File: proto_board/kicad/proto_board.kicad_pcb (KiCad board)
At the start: 2 copper layers, 66 x 100 mm, 3 parts, among them J1 pcie_98, J2 Conn_02x25_Odd_Even, J3 Conn_02x25_Odd_Even

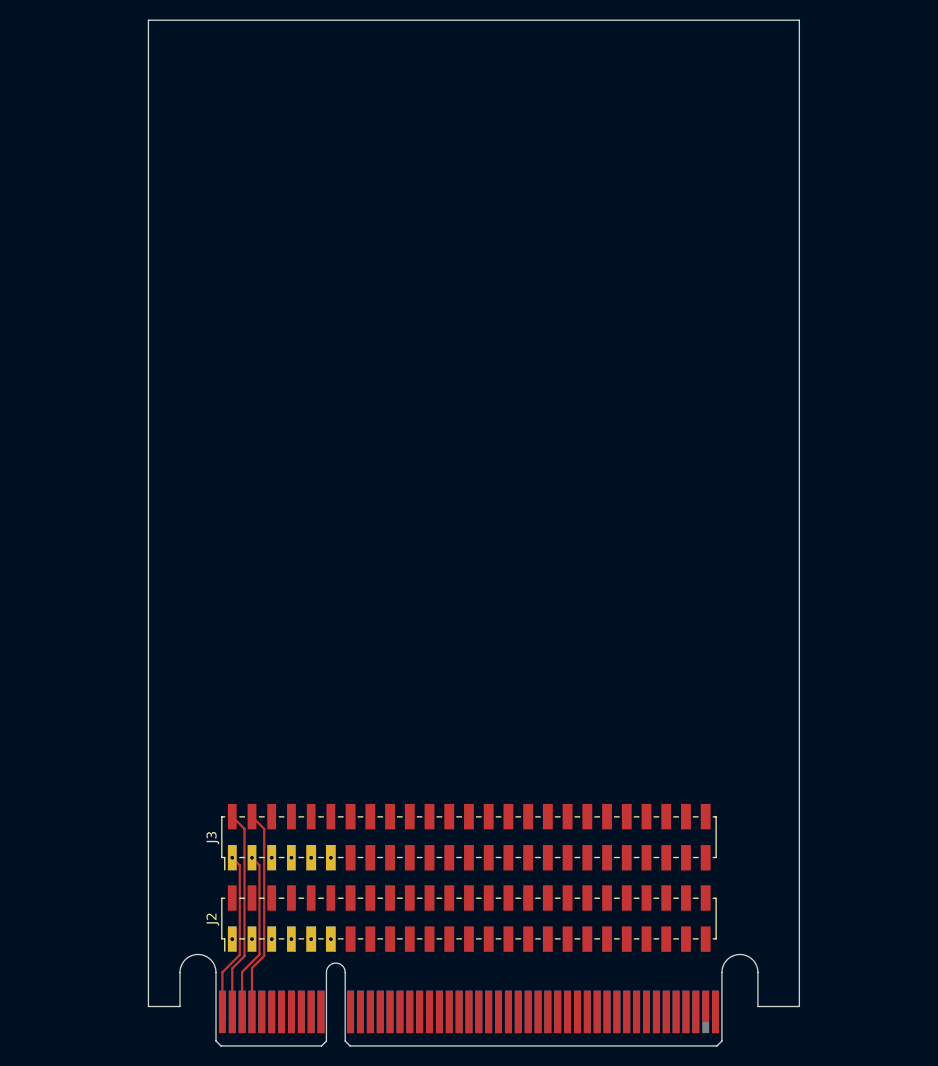
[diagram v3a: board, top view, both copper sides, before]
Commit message: Resized the proto board and added pads grid.
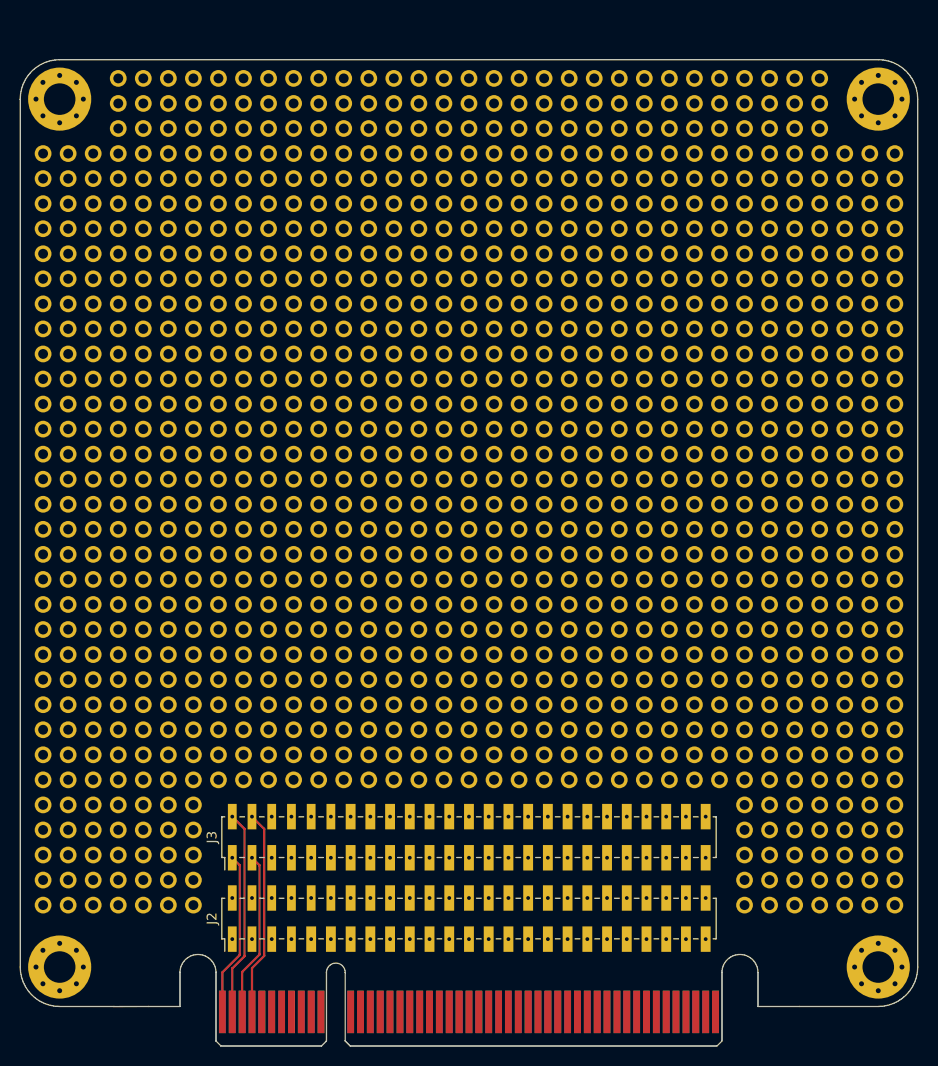
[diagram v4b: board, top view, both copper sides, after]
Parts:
- added H1: MountingHole, MountingHole:MountingHole_3.2mm_M3_Pad_Via, F.Cu at (-28.0, -96.0)
- added H2: MountingHole, MountingHole:MountingHole_3.2mm_M3_Pad_Via, F.Cu at (55.0, -96.0)
- added H3: MountingHole, MountingHole:MountingHole_3.2mm_M3_Pad_Via, F.Cu at (-28.0, -8.00)
- added H4: MountingHole, MountingHole:MountingHole_3.2mm_M3_Pad_Via, F.Cu at (55.0, -8.00)
- added REF**: pad, proto_board:pad, F.Cu at (26.2, -70.2)
- added REF**: pad, proto_board:pad, F.Cu at (-14.4, -24.4)
- added REF**: pad, proto_board:pad, F.Cu at (41.4, -27.0)
- added REF**: pad, proto_board:pad, F.Cu at (46.5, -54.9)
- added REF**: pad, proto_board:pad, F.Cu at (-24.6, -32.1)
- added REF**: pad, proto_board:pad, F.Cu at (23.7, -32.1)
- added REF**: pad, proto_board:pad, F.Cu at (-4.28, -87.9)
- added REF**: pad, proto_board:pad, F.Cu at (46.5, -75.2)
- added REF**: pad, proto_board:pad, F.Cu at (0.80, -82.9)
- added REF**: pad, proto_board:pad, F.Cu at (-17.0, -62.5)
- added REF**: pad, proto_board:pad, F.Cu at (3.34, -65.1)
- added REF**: pad, proto_board:pad, F.Cu at (13.5, -70.2)
- added REF**: pad, proto_board:pad, F.Cu at (51.6, -90.5)
- added REF**: pad, proto_board:pad, F.Cu at (51.6, -47.3)
- added REF**: pad, proto_board:pad, F.Cu at (-14.4, -95.6)
- added REF**: pad, proto_board:pad, F.Cu at (46.5, -52.4)
- added REF**: pad, proto_board:pad, F.Cu at (-22.1, -32.1)
- added REF**: pad, proto_board:pad, F.Cu at (-9.36, -47.3)
- added REF**: pad, proto_board:pad, F.Cu at (41.4, -57.5)
- added REF**: pad, proto_board:pad, F.Cu at (-19.5, -34.6)
- added REF**: pad, proto_board:pad, F.Cu at (44.0, -65.1)
- added REF**: pad, proto_board:pad, F.Cu at (38.9, -70.2)
- added REF**: pad, proto_board:pad, F.Cu at (-24.6, -75.2)
- added REF**: pad, proto_board:pad, F.Cu at (-14.4, -93.0)
- added REF**: pad, proto_board:pad, F.Cu at (21.1, -57.5)
- added REF**: pad, proto_board:pad, F.Cu at (36.4, -44.8)
- added REF**: pad, proto_board:pad, F.Cu at (26.2, -62.5)
- added REF**: pad, proto_board:pad, F.Cu at (-27.1, -29.5)
- added REF**: pad, proto_board:pad, F.Cu at (13.5, -80.3)
- added REF**: pad, proto_board:pad, F.Cu at (36.4, -80.3)
- added REF**: pad, proto_board:pad, F.Cu at (11.0, -34.6)
- added REF**: pad, proto_board:pad, F.Cu at (33.8, -93.0)
- added REF**: pad, proto_board:pad, F.Cu at (46.5, -29.5)
- added REF**: pad, proto_board:pad, F.Cu at (28.7, -62.5)
- added REF**: pad, proto_board:pad, F.Cu at (-11.9, -77.8)
- added REF**: pad, proto_board:pad, F.Cu at (54.1, -54.9)
- added REF**: pad, proto_board:pad, F.Cu at (-11.9, -42.2)
- added REF**: pad, proto_board:pad, F.Cu at (51.6, -27.0)
- added REF**: pad, proto_board:pad, F.Cu at (21.1, -87.9)
- added REF**: pad, proto_board:pad, F.Cu at (0.80, -32.1)
- added REF**: pad, proto_board:pad, F.Cu at (54.1, -82.9)
- added REF**: pad, proto_board:pad, F.Cu at (-27.1, -19.4)
- added REF**: pad, proto_board:pad, F.Cu at (-22.1, -72.7)
- added REF**: pad, proto_board:pad, F.Cu at (41.4, -54.9)
- added REF**: pad, proto_board:pad, F.Cu at (44.0, -85.4)
- added REF**: pad, proto_board:pad, F.Cu at (28.7, -85.4)
- added REF**: pad, proto_board:pad, F.Cu at (-9.36, -37.1)
- added REF**: pad, proto_board:pad, F.Cu at (56.7, -49.8)
- added REF**: pad, proto_board:pad, F.Cu at (5.88, -27.0)
- added REF**: pad, proto_board:pad, F.Cu at (26.2, -67.6)
- added REF**: pad, proto_board:pad, F.Cu at (-14.4, -39.7)
- added REF**: pad, proto_board:pad, F.Cu at (36.4, -90.5)
- added REF**: pad, proto_board:pad, F.Cu at (51.6, -60.0)
- added REF**: pad, proto_board:pad, F.Cu at (-29.7, -21.9)
- added REF**: pad, proto_board:pad, F.Cu at (56.7, -14.3)
- added REF**: pad, proto_board:pad, F.Cu at (-27.1, -37.1)
- added REF**: pad, proto_board:pad, F.Cu at (49.1, -77.8)
- added REF**: pad, proto_board:pad, F.Cu at (41.4, -67.6)
- added REF**: pad, proto_board:pad, F.Cu at (21.1, -70.2)
- added REF**: pad, proto_board:pad, F.Cu at (5.88, -87.9)
- added REF**: pad, proto_board:pad, F.Cu at (13.5, -62.5)
- added REF**: pad, proto_board:pad, F.Cu at (51.6, -52.4)
- added REF**: pad, proto_board:pad, F.Cu at (8.42, -57.5)
- added REF**: pad, proto_board:pad, F.Cu at (5.88, -77.8)
- added REF**: pad, proto_board:pad, F.Cu at (-27.1, -85.4)
- added REF**: pad, proto_board:pad, F.Cu at (44.0, -49.8)
- added REF**: pad, proto_board:pad, F.Cu at (18.6, -42.2)
- added REF**: pad, proto_board:pad, F.Cu at (18.6, -70.2)
- added REF**: pad, proto_board:pad, F.Cu at (-24.6, -87.9)
- added REF**: pad, proto_board:pad, F.Cu at (13.5, -57.5)
- added REF**: pad, proto_board:pad, F.Cu at (11.0, -52.4)
- added REF**: pad, proto_board:pad, F.Cu at (26.2, -44.8)
- added REF**: pad, proto_board:pad, F.Cu at (44.0, -27.0)
- added REF**: pad, proto_board:pad, F.Cu at (23.7, -47.3)
- added REF**: pad, proto_board:pad, F.Cu at (26.2, -57.5)
- added REF**: pad, proto_board:pad, F.Cu at (-19.5, -72.7)
- added REF**: pad, proto_board:pad, F.Cu at (-14.4, -49.8)
- added REF**: pad, proto_board:pad, F.Cu at (-19.5, -82.9)
- added REF**: pad, proto_board:pad, F.Cu at (38.9, -52.4)
- added REF**: pad, proto_board:pad, F.Cu at (-4.28, -34.6)
- added REF**: pad, proto_board:pad, F.Cu at (-29.7, -65.1)
- added REF**: pad, proto_board:pad, F.Cu at (13.5, -72.7)
- added REF**: pad, proto_board:pad, F.Cu at (21.1, -75.2)
- added REF**: pad, proto_board:pad, F.Cu at (31.3, -72.7)
- added REF**: pad, proto_board:pad, F.Cu at (46.5, -82.9)
- added REF**: pad, proto_board:pad, F.Cu at (-27.1, -72.7)
- added REF**: pad, proto_board:pad, F.Cu at (41.4, -44.8)
- added REF**: pad, proto_board:pad, F.Cu at (56.7, -82.9)
- added REF**: pad, proto_board:pad, F.Cu at (38.9, -32.1)
- added REF**: pad, proto_board:pad, F.Cu at (-9.36, -42.2)
- added REF**: pad, proto_board:pad, F.Cu at (11.0, -82.9)
- added REF**: pad, proto_board:pad, F.Cu at (-27.1, -77.8)
- added REF**: pad, proto_board:pad, F.Cu at (-24.6, -67.6)
- added REF**: pad, proto_board:pad, F.Cu at (-11.9, -49.8)
- added REF**: pad, proto_board:pad, F.Cu at (-22.1, -57.5)
- added REF**: pad, proto_board:pad, F.Cu at (-29.7, -52.4)
- added REF**: pad, proto_board:pad, F.Cu at (-14.4, -90.5)
- added REF**: pad, proto_board:pad, F.Cu at (51.6, -80.3)
- added REF**: pad, proto_board:pad, F.Cu at (16.0, -39.7)
- added REF**: pad, proto_board:pad, F.Cu at (54.1, -49.8)
- added REF**: pad, proto_board:pad, F.Cu at (31.3, -62.5)
- added REF**: pad, proto_board:pad, F.Cu at (38.9, -37.1)
- added REF**: pad, proto_board:pad, F.Cu at (8.42, -75.2)
- added REF**: pad, proto_board:pad, F.Cu at (44.0, -14.3)
- added REF**: pad, proto_board:pad, F.Cu at (-6.82, -39.7)
- added REF**: pad, proto_board:pad, F.Cu at (46.5, -95.6)
- added REF**: pad, proto_board:pad, F.Cu at (23.7, -62.5)
- added REF**: pad, proto_board:pad, F.Cu at (5.88, -49.8)
- added REF**: pad, proto_board:pad, F.Cu at (13.5, -98.1)
- added REF**: pad, proto_board:pad, F.Cu at (0.80, -90.5)
- added REF**: pad, proto_board:pad, F.Cu at (5.88, -75.2)
- added REF**: pad, proto_board:pad, F.Cu at (-19.5, -39.7)
- added REF**: pad, proto_board:pad, F.Cu at (-1.74, -57.5)
- added REF**: pad, proto_board:pad, F.Cu at (-11.9, -34.6)
- added REF**: pad, proto_board:pad, F.Cu at (49.1, -93.0)
- added REF**: pad, proto_board:pad, F.Cu at (-19.5, -16.8)
- added REF**: pad, proto_board:pad, F.Cu at (-6.82, -27.0)
- added REF**: pad, proto_board:pad, F.Cu at (-6.82, -80.3)
- added REF**: pad, proto_board:pad, F.Cu at (36.4, -49.8)
- added REF**: pad, proto_board:pad, F.Cu at (23.7, -70.2)
- added REF**: pad, proto_board:pad, F.Cu at (-11.9, -85.4)
- added REF**: pad, proto_board:pad, F.Cu at (-17.0, -87.9)
- added REF**: pad, proto_board:pad, F.Cu at (-9.36, -44.8)
- added REF**: pad, proto_board:pad, F.Cu at (49.1, -72.7)
- added REF**: pad, proto_board:pad, F.Cu at (18.6, -72.7)
- added REF**: pad, proto_board:pad, F.Cu at (41.4, -82.9)
- added REF**: pad, proto_board:pad, F.Cu at (21.1, -72.7)
- added REF**: pad, proto_board:pad, F.Cu at (-22.1, -98.1)
- added REF**: pad, proto_board:pad, F.Cu at (23.7, -65.1)
- added REF**: pad, proto_board:pad, F.Cu at (-17.0, -27.0)
- added REF**: pad, proto_board:pad, F.Cu at (-24.6, -27.0)
- added REF**: pad, proto_board:pad, F.Cu at (41.4, -29.5)
- added REF**: pad, proto_board:pad, F.Cu at (49.1, -19.4)
- added REF**: pad, proto_board:pad, F.Cu at (-29.7, -44.8)
- added REF**: pad, proto_board:pad, F.Cu at (-9.36, -85.4)
- added REF**: pad, proto_board:pad, F.Cu at (23.7, -85.4)
- added REF**: pad, proto_board:pad, F.Cu at (-9.36, -72.7)
- added REF**: pad, proto_board:pad, F.Cu at (26.2, -60.0)
- added REF**: pad, proto_board:pad, F.Cu at (18.6, -37.1)
- added REF**: pad, proto_board:pad, F.Cu at (33.8, -90.5)
- added REF**: pad, proto_board:pad, F.Cu at (-1.74, -77.8)
- added REF**: pad, proto_board:pad, F.Cu at (46.5, -49.8)
- added REF**: pad, proto_board:pad, F.Cu at (54.1, -62.5)
- added REF**: pad, proto_board:pad, F.Cu at (49.1, -34.6)
- added REF**: pad, proto_board:pad, F.Cu at (3.34, -32.1)
- added REF**: pad, proto_board:pad, F.Cu at (3.34, -87.9)
- added REF**: pad, proto_board:pad, F.Cu at (5.88, -65.1)
- added REF**: pad, proto_board:pad, F.Cu at (46.5, -62.5)
- added REF**: pad, proto_board:pad, F.Cu at (-1.74, -52.4)
- added REF**: pad, proto_board:pad, F.Cu at (41.4, -49.8)
- added REF**: pad, proto_board:pad, F.Cu at (5.88, -29.5)
- added REF**: pad, proto_board:pad, F.Cu at (-11.9, -60.0)
- added REF**: pad, proto_board:pad, F.Cu at (-17.0, -42.2)
- added REF**: pad, proto_board:pad, F.Cu at (8.42, -70.2)
- added REF**: pad, proto_board:pad, F.Cu at (49.1, -54.9)
- added REF**: pad, proto_board:pad, F.Cu at (28.7, -44.8)
- added REF**: pad, proto_board:pad, F.Cu at (-22.1, -24.4)
- added REF**: pad, proto_board:pad, F.Cu at (49.1, -16.8)
- added REF**: pad, proto_board:pad, F.Cu at (26.2, -37.1)
- added REF**: pad, proto_board:pad, F.Cu at (0.80, -67.6)
- added REF**: pad, proto_board:pad, F.Cu at (26.2, -72.7)
- added REF**: pad, proto_board:pad, F.Cu at (49.1, -95.6)
- added REF**: pad, proto_board:pad, F.Cu at (33.8, -44.8)
- added REF**: pad, proto_board:pad, F.Cu at (16.0, -42.2)
- added REF**: pad, proto_board:pad, F.Cu at (54.1, -44.8)
- added REF**: pad, proto_board:pad, F.Cu at (26.2, -49.8)
- added REF**: pad, proto_board:pad, F.Cu at (54.1, -34.6)
- added REF**: pad, proto_board:pad, F.Cu at (-11.9, -44.8)
- added REF**: pad, proto_board:pad, F.Cu at (-14.4, -54.9)
- added REF**: pad, proto_board:pad, F.Cu at (8.42, -47.3)
- added REF**: pad, proto_board:pad, F.Cu at (-22.1, -16.8)
- added REF**: pad, proto_board:pad, F.Cu at (-4.28, -37.1)
- added REF**: pad, proto_board:pad, F.Cu at (13.5, -77.8)
- added REF**: pad, proto_board:pad, F.Cu at (44.0, -93.0)
- added REF**: pad, proto_board:pad, F.Cu at (-4.28, -52.4)
- added REF**: pad, proto_board:pad, F.Cu at (-4.28, -62.5)
- added REF**: pad, proto_board:pad, F.Cu at (16.0, -93.0)
- added REF**: pad, proto_board:pad, F.Cu at (-29.7, -14.3)
- added REF**: pad, proto_board:pad, F.Cu at (13.5, -27.0)
- added REF**: pad, proto_board:pad, F.Cu at (23.7, -72.7)
- added REF**: pad, proto_board:pad, F.Cu at (51.6, -39.7)
- added REF**: pad, proto_board:pad, F.Cu at (-27.1, -57.5)
- added REF**: pad, proto_board:pad, F.Cu at (-1.74, -42.2)
- added REF**: pad, proto_board:pad, F.Cu at (-22.1, -27.0)
- added REF**: pad, proto_board:pad, F.Cu at (36.4, -42.2)
- added REF**: pad, proto_board:pad, F.Cu at (49.1, -47.3)
- added REF**: pad, proto_board:pad, F.Cu at (-14.4, -80.3)
- added REF**: pad, proto_board:pad, F.Cu at (-9.36, -32.1)
- added REF**: pad, proto_board:pad, F.Cu at (-14.4, -32.1)
- added REF**: pad, proto_board:pad, F.Cu at (44.0, -44.8)
- added REF**: pad, proto_board:pad, F.Cu at (-6.82, -32.1)
- added REF**: pad, proto_board:pad, F.Cu at (-14.4, -85.4)
- added REF**: pad, proto_board:pad, F.Cu at (38.9, -27.0)
- added REF**: pad, proto_board:pad, F.Cu at (-9.36, -52.4)
- added REF**: pad, proto_board:pad, F.Cu at (11.0, -87.9)
- added REF**: pad, proto_board:pad, F.Cu at (-24.6, -42.2)
- added REF**: pad, proto_board:pad, F.Cu at (18.6, -54.9)
- added REF**: pad, proto_board:pad, F.Cu at (0.80, -98.1)
- added REF**: pad, proto_board:pad, F.Cu at (-29.7, -60.0)
- added REF**: pad, proto_board:pad, F.Cu at (36.4, -98.1)
- added REF**: pad, proto_board:pad, F.Cu at (0.80, -65.1)
- added REF**: pad, proto_board:pad, F.Cu at (46.5, -44.8)
- added REF**: pad, proto_board:pad, F.Cu at (28.7, -93.0)
- added REF**: pad, proto_board:pad, F.Cu at (-9.36, -54.9)
- added REF**: pad, proto_board:pad, F.Cu at (33.8, -57.5)
- added REF**: pad, proto_board:pad, F.Cu at (31.3, -32.1)
- added REF**: pad, proto_board:pad, F.Cu at (-27.1, -39.7)
- added REF**: pad, proto_board:pad, F.Cu at (-6.82, -42.2)
- added REF**: pad, proto_board:pad, F.Cu at (-11.9, -65.1)
- added REF**: pad, proto_board:pad, F.Cu at (49.1, -57.5)
- added REF**: pad, proto_board:pad, F.Cu at (33.8, -77.8)
- added REF**: pad, proto_board:pad, F.Cu at (26.2, -85.4)
- added REF**: pad, proto_board:pad, F.Cu at (-19.5, -98.1)
- added REF**: pad, proto_board:pad, F.Cu at (3.34, -80.3)
- added REF**: pad, proto_board:pad, F.Cu at (36.4, -95.6)
- added REF**: pad, proto_board:pad, F.Cu at (-1.74, -47.3)
- added REF**: pad, proto_board:pad, F.Cu at (8.42, -39.7)
- added REF**: pad, proto_board:pad, F.Cu at (5.88, -62.5)
- added REF**: pad, proto_board:pad, F.Cu at (28.7, -75.2)
- added REF**: pad, proto_board:pad, F.Cu at (-22.1, -70.2)
- added REF**: pad, proto_board:pad, F.Cu at (33.8, -72.7)
- added REF**: pad, proto_board:pad, F.Cu at (-1.74, -65.1)
- added REF**: pad, proto_board:pad, F.Cu at (46.5, -57.5)
- added REF**: pad, proto_board:pad, F.Cu at (-11.9, -82.9)
- added REF**: pad, proto_board:pad, F.Cu at (51.6, -37.1)
- added REF**: pad, proto_board:pad, F.Cu at (-4.28, -82.9)
- added REF**: pad, proto_board:pad, F.Cu at (28.7, -60.0)
- added REF**: pad, proto_board:pad, F.Cu at (-14.4, -14.3)
- added REF**: pad, proto_board:pad, F.Cu at (13.5, -54.9)
- added REF**: pad, proto_board:pad, F.Cu at (-29.7, -34.6)
- added REF**: pad, proto_board:pad, F.Cu at (-9.36, -93.0)
- added REF**: pad, proto_board:pad, F.Cu at (38.9, -47.3)
- added REF**: pad, proto_board:pad, F.Cu at (-17.0, -29.5)
- added REF**: pad, proto_board:pad, F.Cu at (46.5, -87.9)
- added REF**: pad, proto_board:pad, F.Cu at (3.34, -34.6)
- added REF**: pad, proto_board:pad, F.Cu at (31.3, -49.8)
- added REF**: pad, proto_board:pad, F.Cu at (21.1, -93.0)
- added REF**: pad, proto_board:pad, F.Cu at (21.1, -44.8)
- added REF**: pad, proto_board:pad, F.Cu at (3.34, -70.2)
- added REF**: pad, proto_board:pad, F.Cu at (49.1, -62.5)
- added REF**: pad, proto_board:pad, F.Cu at (-6.82, -93.0)
- added REF**: pad, proto_board:pad, F.Cu at (54.1, -90.5)
- added REF**: pad, proto_board:pad, F.Cu at (23.7, -82.9)
- added REF**: pad, proto_board:pad, F.Cu at (54.1, -42.2)
- added REF**: pad, proto_board:pad, F.Cu at (56.7, -67.6)
- added REF**: pad, proto_board:pad, F.Cu at (36.4, -67.6)
- added REF**: pad, proto_board:pad, F.Cu at (11.0, -98.1)
- added REF**: pad, proto_board:pad, F.Cu at (18.6, -34.6)
- added REF**: pad, proto_board:pad, F.Cu at (38.9, -65.1)
- added REF**: pad, proto_board:pad, F.Cu at (51.6, -75.2)
- added REF**: pad, proto_board:pad, F.Cu at (28.7, -42.2)
- added REF**: pad, proto_board:pad, F.Cu at (8.42, -77.8)
- added REF**: pad, proto_board:pad, F.Cu at (31.3, -85.4)
- added REF**: pad, proto_board:pad, F.Cu at (13.5, -52.4)
- added REF**: pad, proto_board:pad, F.Cu at (54.1, -47.3)
- added REF**: pad, proto_board:pad, F.Cu at (-19.5, -19.4)
- added REF**: pad, proto_board:pad, F.Cu at (54.1, -72.7)
- added REF**: pad, proto_board:pad, F.Cu at (-1.74, -85.4)
- added REF**: pad, proto_board:pad, F.Cu at (11.0, -42.2)
- added REF**: pad, proto_board:pad, F.Cu at (-4.28, -32.1)
- added REF**: pad, proto_board:pad, F.Cu at (21.1, -47.3)
- added REF**: pad, proto_board:pad, F.Cu at (41.4, -16.8)
- added REF**: pad, proto_board:pad, F.Cu at (38.9, -29.5)
- added REF**: pad, proto_board:pad, F.Cu at (36.4, -57.5)
- added REF**: pad, proto_board:pad, F.Cu at (44.0, -29.5)
- added REF**: pad, proto_board:pad, F.Cu at (38.9, -95.6)
- added REF**: pad, proto_board:pad, F.Cu at (16.0, -54.9)
- added REF**: pad, proto_board:pad, F.Cu at (38.9, -57.5)
- added REF**: pad, proto_board:pad, F.Cu at (28.7, -95.6)
- added REF**: pad, proto_board:pad, F.Cu at (-17.0, -39.7)
- added REF**: pad, proto_board:pad, F.Cu at (8.42, -93.0)
- added REF**: pad, proto_board:pad, F.Cu at (18.6, -60.0)
- added REF**: pad, proto_board:pad, F.Cu at (-1.74, -75.2)
- added REF**: pad, proto_board:pad, F.Cu at (-11.9, -98.1)
- added REF**: pad, proto_board:pad, F.Cu at (3.34, -60.0)
- added REF**: pad, proto_board:pad, F.Cu at (38.9, -87.9)
- added REF**: pad, proto_board:pad, F.Cu at (21.1, -98.1)
- added REF**: pad, proto_board:pad, F.Cu at (26.2, -75.2)
- added REF**: pad, proto_board:pad, F.Cu at (-17.0, -85.4)
- added REF**: pad, proto_board:pad, F.Cu at (51.6, -62.5)
- added REF**: pad, proto_board:pad, F.Cu at (8.42, -42.2)
- added REF**: pad, proto_board:pad, F.Cu at (-14.4, -98.1)
- added REF**: pad, proto_board:pad, F.Cu at (41.4, -52.4)
- added REF**: pad, proto_board:pad, F.Cu at (0.80, -52.4)
- added REF**: pad, proto_board:pad, F.Cu at (18.6, -90.5)
- added REF**: pad, proto_board:pad, F.Cu at (51.6, -32.1)
- added REF**: pad, proto_board:pad, F.Cu at (49.1, -67.6)
- added REF**: pad, proto_board:pad, F.Cu at (16.0, -77.8)
- added REF**: pad, proto_board:pad, F.Cu at (-24.6, -62.5)
- added REF**: pad, proto_board:pad, F.Cu at (41.4, -47.3)
- added REF**: pad, proto_board:pad, F.Cu at (-19.5, -37.1)
- added REF**: pad, proto_board:pad, F.Cu at (11.0, -39.7)
- added REF**: pad, proto_board:pad, F.Cu at (31.3, -87.9)
- added REF**: pad, proto_board:pad, F.Cu at (-27.1, -24.4)
- added REF**: pad, proto_board:pad, F.Cu at (11.0, -47.3)
- added REF**: pad, proto_board:pad, F.Cu at (26.2, -95.6)
- added REF**: pad, proto_board:pad, F.Cu at (28.7, -87.9)
- added REF**: pad, proto_board:pad, F.Cu at (8.42, -62.5)
- added REF**: pad, proto_board:pad, F.Cu at (-19.5, -27.0)
- added REF**: pad, proto_board:pad, F.Cu at (-1.74, -32.1)
- added REF**: pad, proto_board:pad, F.Cu at (56.7, -57.5)
- added REF**: pad, proto_board:pad, F.Cu at (18.6, -47.3)
- added REF**: pad, proto_board:pad, F.Cu at (44.0, -19.4)
- added REF**: pad, proto_board:pad, F.Cu at (56.7, -60.0)
- added REF**: pad, proto_board:pad, F.Cu at (23.7, -80.3)
- added REF**: pad, proto_board:pad, F.Cu at (51.6, -70.2)
- added REF**: pad, proto_board:pad, F.Cu at (44.0, -72.7)
- added REF**: pad, proto_board:pad, F.Cu at (-27.1, -44.8)
- added REF**: pad, proto_board:pad, F.Cu at (36.4, -52.4)
- added REF**: pad, proto_board:pad, F.Cu at (21.1, -37.1)
- added REF**: pad, proto_board:pad, F.Cu at (36.4, -32.1)
- added REF**: pad, proto_board:pad, F.Cu at (56.7, -21.9)
- added REF**: pad, proto_board:pad, F.Cu at (0.80, -95.6)
- added REF**: pad, proto_board:pad, F.Cu at (46.5, -34.6)
- added REF**: pad, proto_board:pad, F.Cu at (33.8, -32.1)
- added REF**: pad, proto_board:pad, F.Cu at (-22.1, -93.0)
- added REF**: pad, proto_board:pad, F.Cu at (-9.36, -67.6)
- added REF**: pad, proto_board:pad, F.Cu at (-24.6, -65.1)
- added REF**: pad, proto_board:pad, F.Cu at (-17.0, -65.1)
- added REF**: pad, proto_board:pad, F.Cu at (5.88, -67.6)
- added REF**: pad, proto_board:pad, F.Cu at (41.4, -21.9)
- added REF**: pad, proto_board:pad, F.Cu at (-14.4, -57.5)
- added REF**: pad, proto_board:pad, F.Cu at (-17.0, -90.5)
- added REF**: pad, proto_board:pad, F.Cu at (-24.6, -72.7)
- added REF**: pad, proto_board:pad, F.Cu at (3.34, -49.8)
- added REF**: pad, proto_board:pad, F.Cu at (51.6, -44.8)
- added REF**: pad, proto_board:pad, F.Cu at (-29.7, -57.5)
- added REF**: pad, proto_board:pad, F.Cu at (-22.1, -65.1)
- added REF**: pad, proto_board:pad, F.Cu at (18.6, -62.5)
- added REF**: pad, proto_board:pad, F.Cu at (-22.1, -21.9)
- added REF**: pad, proto_board:pad, F.Cu at (13.5, -82.9)
- added REF**: pad, proto_board:pad, F.Cu at (38.9, -60.0)
- added REF**: pad, proto_board:pad, F.Cu at (-29.7, -75.2)
- added REF**: pad, proto_board:pad, F.Cu at (54.1, -67.6)
- added REF**: pad, proto_board:pad, F.Cu at (-11.9, -52.4)
- added REF**: pad, proto_board:pad, F.Cu at (-24.6, -14.3)
- added REF**: pad, proto_board:pad, F.Cu at (56.7, -37.1)
- added REF**: pad, proto_board:pad, F.Cu at (49.1, -52.4)
- added REF**: pad, proto_board:pad, F.Cu at (18.6, -85.4)
- added REF**: pad, proto_board:pad, F.Cu at (18.6, -49.8)
- added REF**: pad, proto_board:pad, F.Cu at (38.9, -54.9)
- added REF**: pad, proto_board:pad, F.Cu at (-1.74, -87.9)
- added REF**: pad, proto_board:pad, F.Cu at (-29.7, -16.8)
- added REF**: pad, proto_board:pad, F.Cu at (38.9, -93.0)
- added REF**: pad, proto_board:pad, F.Cu at (28.7, -39.7)
- added REF**: pad, proto_board:pad, F.Cu at (-9.36, -62.5)
- added REF**: pad, proto_board:pad, F.Cu at (21.1, -67.6)
- added REF**: pad, proto_board:pad, F.Cu at (54.1, -70.2)
- added REF**: pad, proto_board:pad, F.Cu at (49.1, -90.5)
- added REF**: pad, proto_board:pad, F.Cu at (46.5, -60.0)
- added REF**: pad, proto_board:pad, F.Cu at (26.2, -52.4)
- added REF**: pad, proto_board:pad, F.Cu at (-17.0, -44.8)
- added REF**: pad, proto_board:pad, F.Cu at (5.88, -34.6)
- added REF**: pad, proto_board:pad, F.Cu at (18.6, -44.8)
- added REF**: pad, proto_board:pad, F.Cu at (-17.0, -60.0)
- added REF**: pad, proto_board:pad, F.Cu at (-19.5, -95.6)
- added REF**: pad, proto_board:pad, F.Cu at (26.2, -90.5)
- added REF**: pad, proto_board:pad, F.Cu at (-14.4, -87.9)
- added REF**: pad, proto_board:pad, F.Cu at (33.8, -34.6)
- added REF**: pad, proto_board:pad, F.Cu at (56.7, -65.1)
- added REF**: pad, proto_board:pad, F.Cu at (56.7, -39.7)
- added REF**: pad, proto_board:pad, F.Cu at (8.42, -87.9)
- added REF**: pad, proto_board:pad, F.Cu at (41.4, -65.1)
- added REF**: pad, proto_board:pad, F.Cu at (-1.74, -49.8)
- added REF**: pad, proto_board:pad, F.Cu at (-22.1, -14.3)
- added REF**: pad, proto_board:pad, F.Cu at (51.6, -34.6)
- added REF**: pad, proto_board:pad, F.Cu at (-17.0, -82.9)
- added REF**: pad, proto_board:pad, F.Cu at (8.42, -80.3)
- added REF**: pad, proto_board:pad, F.Cu at (13.5, -44.8)
- added REF**: pad, proto_board:pad, F.Cu at (51.6, -24.4)
- added REF**: pad, proto_board:pad, F.Cu at (49.1, -29.5)
- added REF**: pad, proto_board:pad, F.Cu at (-4.28, -42.2)
- added REF**: pad, proto_board:pad, F.Cu at (-4.28, -80.3)
- added REF**: pad, proto_board:pad, F.Cu at (8.42, -27.0)
- added REF**: pad, proto_board:pad, F.Cu at (46.5, -72.7)
- added REF**: pad, proto_board:pad, F.Cu at (23.7, -34.6)
- added REF**: pad, proto_board:pad, F.Cu at (23.7, -29.5)
- added REF**: pad, proto_board:pad, F.Cu at (-9.36, -77.8)
- added REF**: pad, proto_board:pad, F.Cu at (21.1, -29.5)
- added REF**: pad, proto_board:pad, F.Cu at (54.1, -37.1)
- added REF**: pad, proto_board:pad, F.Cu at (3.34, -57.5)
- added REF**: pad, proto_board:pad, F.Cu at (51.6, -72.7)
- added REF**: pad, proto_board:pad, F.Cu at (-17.0, -34.6)
- added REF**: pad, proto_board:pad, F.Cu at (-14.4, -47.3)
- added REF**: pad, proto_board:pad, F.Cu at (-17.0, -80.3)
- added REF**: pad, proto_board:pad, F.Cu at (41.4, -34.6)
- added REF**: pad, proto_board:pad, F.Cu at (33.8, -49.8)
- added REF**: pad, proto_board:pad, F.Cu at (-9.36, -95.6)
- added REF**: pad, proto_board:pad, F.Cu at (49.1, -80.3)
- added REF**: pad, proto_board:pad, F.Cu at (11.0, -27.0)
- added REF**: pad, proto_board:pad, F.Cu at (-27.1, -49.8)
- added REF**: pad, proto_board:pad, F.Cu at (-27.1, -21.9)
- added REF**: pad, proto_board:pad, F.Cu at (-29.7, -90.5)
- added REF**: pad, proto_board:pad, F.Cu at (-1.74, -60.0)
- added REF**: pad, proto_board:pad, F.Cu at (-19.5, -70.2)
- added REF**: pad, proto_board:pad, F.Cu at (-27.1, -70.2)
- added REF**: pad, proto_board:pad, F.Cu at (-22.1, -19.4)
- added REF**: pad, proto_board:pad, F.Cu at (-14.4, -75.2)
- added REF**: pad, proto_board:pad, F.Cu at (-1.74, -54.9)
- added REF**: pad, proto_board:pad, F.Cu at (-27.1, -60.0)
- added REF**: pad, proto_board:pad, F.Cu at (16.0, -49.8)
- added REF**: pad, proto_board:pad, F.Cu at (-19.5, -80.3)
- added REF**: pad, proto_board:pad, F.Cu at (46.5, -90.5)
- added REF**: pad, proto_board:pad, F.Cu at (54.1, -85.4)
- added REF**: pad, proto_board:pad, F.Cu at (-29.7, -80.3)
- added REF**: pad, proto_board:pad, F.Cu at (41.4, -75.2)
- added REF**: pad, proto_board:pad, F.Cu at (-11.9, -72.7)
- added REF**: pad, proto_board:pad, F.Cu at (18.6, -77.8)
- added REF**: pad, proto_board:pad, F.Cu at (16.0, -57.5)
- added REF**: pad, proto_board:pad, F.Cu at (33.8, -98.1)
- added REF**: pad, proto_board:pad, F.Cu at (-14.4, -29.5)
- added REF**: pad, proto_board:pad, F.Cu at (-6.82, -57.5)
- added REF**: pad, proto_board:pad, F.Cu at (51.6, -65.1)
- added REF**: pad, proto_board:pad, F.Cu at (26.2, -54.9)
- added REF**: pad, proto_board:pad, F.Cu at (-11.9, -32.1)
- added REF**: pad, proto_board:pad, F.Cu at (-22.1, -85.4)
- added REF**: pad, proto_board:pad, F.Cu at (13.5, -60.0)
- added REF**: pad, proto_board:pad, F.Cu at (31.3, -34.6)
- added REF**: pad, proto_board:pad, F.Cu at (26.2, -82.9)
- added REF**: pad, proto_board:pad, F.Cu at (0.80, -62.5)
- added REF**: pad, proto_board:pad, F.Cu at (38.9, -98.1)
- added REF**: pad, proto_board:pad, F.Cu at (-14.4, -34.6)
- added REF**: pad, proto_board:pad, F.Cu at (31.3, -52.4)
- added REF**: pad, proto_board:pad, F.Cu at (-4.28, -57.5)
- added REF**: pad, proto_board:pad, F.Cu at (26.2, -29.5)
- added REF**: pad, proto_board:pad, F.Cu at (-4.28, -95.6)
- added REF**: pad, proto_board:pad, F.Cu at (13.5, -39.7)
- added REF**: pad, proto_board:pad, F.Cu at (21.1, -42.2)
- added REF**: pad, proto_board:pad, F.Cu at (26.2, -77.8)
- added REF**: pad, proto_board:pad, F.Cu at (-6.82, -75.2)
- added REF**: pad, proto_board:pad, F.Cu at (31.3, -77.8)
- added REF**: pad, proto_board:pad, F.Cu at (-29.7, -24.4)
- added REF**: pad, proto_board:pad, F.Cu at (5.88, -85.4)
- added REF**: pad, proto_board:pad, F.Cu at (46.5, -27.0)
- added REF**: pad, proto_board:pad, F.Cu at (49.1, -39.7)
- added REF**: pad, proto_board:pad, F.Cu at (-11.9, -75.2)
- added REF**: pad, proto_board:pad, F.Cu at (44.0, -62.5)
- added REF**: pad, proto_board:pad, F.Cu at (3.34, -72.7)
- added REF**: pad, proto_board:pad, F.Cu at (49.1, -37.1)
- added REF**: pad, proto_board:pad, F.Cu at (-17.0, -21.9)
- added REF**: pad, proto_board:pad, F.Cu at (28.7, -49.8)
- added REF**: pad, proto_board:pad, F.Cu at (36.4, -27.0)
- added REF**: pad, proto_board:pad, F.Cu at (-1.74, -34.6)
- added REF**: pad, proto_board:pad, F.Cu at (3.34, -75.2)
- added REF**: pad, proto_board:pad, F.Cu at (-11.9, -54.9)
- added REF**: pad, proto_board:pad, F.Cu at (0.80, -72.7)
- added REF**: pad, proto_board:pad, F.Cu at (-6.82, -62.5)
- added REF**: pad, proto_board:pad, F.Cu at (16.0, -90.5)
- added REF**: pad, proto_board:pad, F.Cu at (13.5, -32.1)
- added REF**: pad, proto_board:pad, F.Cu at (11.0, -67.6)
- added REF**: pad, proto_board:pad, F.Cu at (31.3, -54.9)
- added REF**: pad, proto_board:pad, F.Cu at (-29.7, -47.3)
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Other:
- board size 66 x 100 mm -> 91 x 96 mm

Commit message: More progress on the schematic. Yet to complete the connectivity.
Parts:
- renumbered J2 to locked, J3 to locked
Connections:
- J1 pad A10: unconnected-(J1-Pin_a10-PadA10) -> /A10
- J1 pad A11: unconnected-(J1-Pin_A11-PadA11) -> /A11
- J1 pad A12: unconnected-(J1-Pin_a12-PadA12) -> /A12
- J1 pad A13: unconnected-(J1-Pin_a13-PadA13) -> /A13
- J1 pad A14: unconnected-(J1-Pin_a14-PadA14) -> /A14
- J1 pad A15: unconnected-(J1-Pin_a15-PadA15) -> /A15
- J1 pad A16: unconnected-(J1-Pin_a16-PadA16) -> /A16
- J1 pad A17: unconnected-(J1-Pin_a17-PadA17) -> /A17
- J1 pad A18: unconnected-(J1-Pin_a18-PadA18) -> /A18
- J1 pad A19: unconnected-(J1-Pin_a19-PadA19) -> /A19
- J1 pad A20: unconnected-(J1-Pin_a20-PadA20) -> /A20
- J1 pad A21: unconnected-(J1-Pin_a21-PadA21) -> /A21
- J1 pad A22: unconnected-(J1-Pin_a22-PadA22) -> /A22
- J1 pad A23: unconnected-(J1-Pin_a23-PadA23) -> /A23
- J1 pad A24: unconnected-(J1-Pin_a24-PadA24) -> /A24
- J1 pad A25: unconnected-(J1-Pin_a25-PadA25) -> /A25
- J1 pad A26: unconnected-(J1-Pin_a26-PadA26) -> /A26
- J1 pad A27: unconnected-(J1-Pin_a27-PadA27) -> /A27
- J1 pad A28: unconnected-(J1-Pin_a28-PadA28) -> /A28
- J1 pad A29: unconnected-(J1-Pin_a29-PadA29) -> /A29
- J1 pad A30: unconnected-(J1-Pin_a30-PadA30) -> /A30
- J1 pad A31: unconnected-(J1-Pin_a31-PadA31) -> /A31
- J1 pad A32: unconnected-(J1-Pin_a32-PadA32) -> /A32
- J1 pad A33: unconnected-(J1-Pin_a33-PadA33) -> /A33
- J1 pad A34: unconnected-(J1-Pin_a34-PadA34) -> /A34
- J1 pad A35: unconnected-(J1-Pin_a35-PadA35) -> /A35
- J1 pad A36: unconnected-(J1-Pin_a36-PadA36) -> /A36
- J1 pad A37: unconnected-(J1-Pin_a37-PadA37) -> /A37
- J1 pad A38: unconnected-(J1-Pin_a38-PadA38) -> /A38
- J1 pad A39: unconnected-(J1-Pin_a39-PadA39) -> /A39
- J1 pad A40: unconnected-(J1-Pin_a40-PadA40) -> /A40
- J1 pad A41: unconnected-(J1-Pin_a41-PadA41) -> /A41
- J1 pad A42: unconnected-(J1-Pin_a42-PadA42) -> /A42
- J1 pad A43: unconnected-(J1-Pin_a43-PadA43) -> /A43
- J1 pad A44: unconnected-(J1-Pin_a44-PadA44) -> /A44
- J1 pad A45: unconnected-(J1-Pin_a45-PadA45) -> /A45
- J1 pad A46: unconnected-(J1-Pin_a46-PadA46) -> /A46
- J1 pad A47: unconnected-(J1-Pin_a47-PadA47) -> /A47
- J1 pad A48: unconnected-(J1-Pin_a48-PadA48) -> /A48
- J1 pad A49: unconnected-(J1-Pin_a49-PadA49) -> /A49
- J1 pad A5: unconnected-(J1-Pin_a5-PadA5) -> /A5
- J1 pad A6: unconnected-(J1-Pin_a6-PadA6) -> /A6
- J1 pad A7: unconnected-(J1-Pin_a7-PadA7) -> /A7
- J1 pad A8: unconnected-(J1-Pin_a8-PadA8) -> /A8
- J1 pad A9: unconnected-(J1-Pin_a9-PadA9) -> /A9
- J1 pad B10: unconnected-(J1-Pin_b10-PadB10) -> /B10
- J1 pad B11: unconnected-(J1-Pin_b11-PadB11) -> /B11
- J1 pad B12: unconnected-(J1-Pin_b12-PadB12) -> /B12
- J1 pad B13: unconnected-(J1-Pin_b13-PadB13) -> /B13
- J1 pad B14: unconnected-(J1-Pin_b14-PadB14) -> /B14
- J1 pad B15: unconnected-(J1-Pin_b15-PadB15) -> /B15
- J1 pad B16: unconnected-(J1-Pin_b16-PadB16) -> /B16
- J1 pad B17: unconnected-(J1-Pin_b17-PadB17) -> /B17
- J1 pad B18: unconnected-(J1-Pin_b18-PadB18) -> /B18
- J1 pad B19: unconnected-(J1-Pin_b19-PadB19) -> /B19
- J1 pad B20: unconnected-(J1-Pin_b20-PadB20) -> /B20
- J1 pad B21: unconnected-(J1-Pin_b21-PadB21) -> /B21
- J1 pad B22: unconnected-(J1-Pin_b22-PadB22) -> /B22
- J1 pad B23: unconnected-(J1-Pin_b23-PadB23) -> /B23
- J1 pad B24: unconnected-(J1-Pin_b24-PadB24) -> /B24
- J1 pad B25: unconnected-(J1-Pin_b25-PadB25) -> /B25
- J1 pad B26: unconnected-(J1-Pin_b26-PadB26) -> /B26
- J1 pad B27: unconnected-(J1-Pin_b27-PadB27) -> /B27
- J1 pad B28: unconnected-(J1-Pin_b28-PadB28) -> /B28
- J1 pad B29: unconnected-(J1-Pin_b29-PadB29) -> /B29
- J1 pad B30: unconnected-(J1-Pin_b30-PadB30) -> /B30
- J1 pad B31: unconnected-(J1-Pin_b31-PadB31) -> /B31
- J1 pad B32: unconnected-(J1-Pin_b32-PadB32) -> /B32
- J1 pad B33: unconnected-(J1-Pin_b33-PadB33) -> /B33
- J1 pad B34: unconnected-(J1-Pin_b34-PadB34) -> /B34
- J1 pad B35: unconnected-(J1-Pin_b35-PadB35) -> /B35
- J1 pad B36: unconnected-(J1-Pin_b36-PadB36) -> /B36
- J1 pad B37: unconnected-(J1-Pin_b37-PadB37) -> /B37
- J1 pad B38: unconnected-(J1-Pin_b38-PadB38) -> /B38
- J1 pad B39: unconnected-(J1-Pin_b39-PadB39) -> /B39
- J1 pad B40: unconnected-(J1-Pin_b40-PadB40) -> /B40
- J1 pad B41: unconnected-(J1-Pin_b41-PadB41) -> /B41
- J1 pad B42: unconnected-(J1-Pin_b42-PadB42) -> /B42
- J1 pad B43: unconnected-(J1-Pin_b43-PadB43) -> /B43
- J1 pad B44: unconnected-(J1-Pin_b44-PadB44) -> /B44
- J1 pad B45: unconnected-(J1-Pin_b45-PadB45) -> /B45
- J1 pad B46: unconnected-(J1-Pin_46-PadB46) -> /B46
- J1 pad B47: unconnected-(J1-Pin_b47-PadB47) -> /B47
- J1 pad B48: unconnected-(J1-Pin_b48-PadB48) -> /B48
- J1 pad B49: unconnected-(J1-Pin_b49-PadB49) -> /B49
- J1 pad B5: unconnected-(J1-Pin_b5-PadB5) -> /B5
- J1 pad B6: unconnected-(J1-Pin_b6-PadB6) -> /B6
- J1 pad B7: unconnected-(J1-Pin_b7-PadB7) -> /B7
- J1 pad B8: unconnected-(J1-Pin_b8-PadB8) -> /B8
- J1 pad B9: unconnected-(J1-Pin_b9-PadB9) -> /B9
- locked pad 10: unconnected-(J2-Pin_10-Pad10) -> /A10
- locked pad 11: unconnected-(J2-Pin_11-Pad11) -> /A11
- locked pad 12: unconnected-(J2-Pin_12-Pad12) -> /A
- locked pad 13: unconnected-(J2-Pin_13-Pad13) -> /A
- locked pad 14: unconnected-(J2-Pin_14-Pad14) -> /A
- locked pad 15: unconnected-(J2-Pin_15-Pad15) -> /A
- locked pad 16: unconnected-(J2-Pin_16-Pad16) -> /A
- locked pad 17: unconnected-(J2-Pin_17-Pad17) -> /A
- locked pad 18: unconnected-(J2-Pin_18-Pad18) -> /A
- locked pad 19: unconnected-(J2-Pin_19-Pad19) -> /A
- locked pad 20: unconnected-(J2-Pin_20-Pad20) -> /A
- locked pad 21: unconnected-(J2-Pin_21-Pad21) -> /A
- locked pad 22: unconnected-(J2-Pin_22-Pad22) -> /A
- locked pad 23: unconnected-(J2-Pin_23-Pad23) -> /A
- locked pad 24: unconnected-(J2-Pin_24-Pad24) -> /A
- locked pad 25: unconnected-(J2-Pin_25-Pad25) -> /A
- locked pad 26: unconnected-(J2-Pin_26-Pad26) -> /A
- locked pad 27: unconnected-(J2-Pin_27-Pad27) -> /A
- locked pad 28: unconnected-(J2-Pin_28-Pad28) -> /A
- locked pad 29: unconnected-(J2-Pin_29-Pad29) -> /A
- locked pad 30: unconnected-(J2-Pin_30-Pad30) -> /A
- locked pad 31: unconnected-(J2-Pin_31-Pad31) -> /A
- locked pad 32: unconnected-(J2-Pin_32-Pad32) -> /A
- locked pad 33: unconnected-(J2-Pin_33-Pad33) -> /A
- locked pad 34: unconnected-(J2-Pin_34-Pad34) -> /A
- locked pad 35: unconnected-(J2-Pin_35-Pad35) -> /A
- locked pad 36: unconnected-(J2-Pin_36-Pad36) -> /A
- locked pad 37: unconnected-(J2-Pin_37-Pad37) -> /A
- locked pad 38: unconnected-(J2-Pin_38-Pad38) -> /A
- locked pad 39: unconnected-(J2-Pin_39-Pad39) -> /A
- locked pad 40: unconnected-(J2-Pin_40-Pad40) -> /A
- locked pad 41: unconnected-(J2-Pin_41-Pad41) -> /A
- locked pad 42: unconnected-(J2-Pin_42-Pad42) -> /A
- locked pad 43: unconnected-(J2-Pin_43-Pad43) -> /A
- locked pad 44: unconnected-(J2-Pin_44-Pad44) -> /A
- locked pad 45: unconnected-(J2-Pin_45-Pad45) -> /A
- locked pad 46: unconnected-(J2-Pin_46-Pad46) -> /A
- locked pad 47: unconnected-(J2-Pin_47-Pad47) -> /A
- locked pad 48: unconnected-(J2-Pin_48-Pad48) -> /A
- locked pad 49: unconnected-(J2-Pin_49-Pad49) -> /A
- locked pad 5: unconnected-(J2-Pin_5-Pad5) -> /A5
- locked pad 50: unconnected-(J2-Pin_50-Pad50) -> /A
- locked pad 6: unconnected-(J2-Pin_6-Pad6) -> /A6
- locked pad 7: unconnected-(J2-Pin_7-Pad7) -> /A7
- locked pad 8: unconnected-(J2-Pin_8-Pad8) -> /A8
- locked pad 9: unconnected-(J2-Pin_9-Pad9) -> /A9
- locked pad 10: unconnected-(J3-Pin_10-Pad10) -> /B10
- locked pad 11: unconnected-(J3-Pin_11-Pad11) -> /B11
- locked pad 12: unconnected-(J3-Pin_12-Pad12) -> /B
- locked pad 13: unconnected-(J3-Pin_13-Pad13) -> /B
- locked pad 14: unconnected-(J3-Pin_14-Pad14) -> /B
- locked pad 15: unconnected-(J3-Pin_15-Pad15) -> /B
- locked pad 16: unconnected-(J3-Pin_16-Pad16) -> /B
- locked pad 17: unconnected-(J3-Pin_17-Pad17) -> /B
- locked pad 18: unconnected-(J3-Pin_18-Pad18) -> /B
- locked pad 19: unconnected-(J3-Pin_19-Pad19) -> /B
- locked pad 20: unconnected-(J3-Pin_20-Pad20) -> /B
- locked pad 21: unconnected-(J3-Pin_21-Pad21) -> /B
- locked pad 22: unconnected-(J3-Pin_22-Pad22) -> /B
- locked pad 23: unconnected-(J3-Pin_23-Pad23) -> /B
- locked pad 24: unconnected-(J3-Pin_24-Pad24) -> /B
- locked pad 25: unconnected-(J3-Pin_25-Pad25) -> /B
- locked pad 26: unconnected-(J3-Pin_26-Pad26) -> /B
- locked pad 27: unconnected-(J3-Pin_27-Pad27) -> /B
- locked pad 28: unconnected-(J3-Pin_28-Pad28) -> /B
- locked pad 29: unconnected-(J3-Pin_29-Pad29) -> /B
- locked pad 30: unconnected-(J3-Pin_30-Pad30) -> /B
- locked pad 31: unconnected-(J3-Pin_31-Pad31) -> /B
- locked pad 32: unconnected-(J3-Pin_32-Pad32) -> /B
- locked pad 33: unconnected-(J3-Pin_33-Pad33) -> /B
- locked pad 34: unconnected-(J3-Pin_34-Pad34) -> /B
- locked pad 35: unconnected-(J3-Pin_35-Pad35) -> /B
- locked pad 36: unconnected-(J3-Pin_36-Pad36) -> /B
- locked pad 37: unconnected-(J3-Pin_37-Pad37) -> /B
- locked pad 38: unconnected-(J3-Pin_38-Pad38) -> /B
- locked pad 39: unconnected-(J3-Pin_39-Pad39) -> /B
- locked pad 40: unconnected-(J3-Pin_40-Pad40) -> /B
- locked pad 41: unconnected-(J3-Pin_41-Pad41) -> /B
- locked pad 42: unconnected-(J3-Pin_42-Pad42) -> /B
- locked pad 43: unconnected-(J3-Pin_43-Pad43) -> /B
- locked pad 44: unconnected-(J3-Pin_44-Pad44) -> /B
- locked pad 45: unconnected-(J3-Pin_45-Pad45) -> /B
- locked pad 46: unconnected-(J3-Pin_46-Pad46) -> /B
- locked pad 47: unconnected-(J3-Pin_47-Pad47) -> /B
- locked pad 48: unconnected-(J3-Pin_48-Pad48) -> /B
- locked pad 49: unconnected-(J3-Pin_49-Pad49) -> /B
- locked pad 5: unconnected-(J3-Pin_5-Pad5) -> /B5
- locked pad 50: unconnected-(J3-Pin_50-Pad50) -> /B
- locked pad 6: unconnected-(J3-Pin_6-Pad6) -> /B6
- locked pad 7: unconnected-(J3-Pin_7-Pad7) -> /B7
- locked pad 8: unconnected-(J3-Pin_8-Pad8) -> /B8
- locked pad 9: unconnected-(J3-Pin_9-Pad9) -> /B9
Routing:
- net /B4: track 20.8 -> 0.00 mm
- net /B2: track 20.8 -> 0.00 mm
- net /B3: track 16.7 -> 0.00 mm
- net /B1: track 16.7 -> 0.00 mm
